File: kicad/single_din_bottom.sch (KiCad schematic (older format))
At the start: 7 parts, among them J1 Conn_01x04, J2 Conn_01x04, J3 Conn_01x04, J4 Conn_01x04, U1 R-78B3.3-2.0

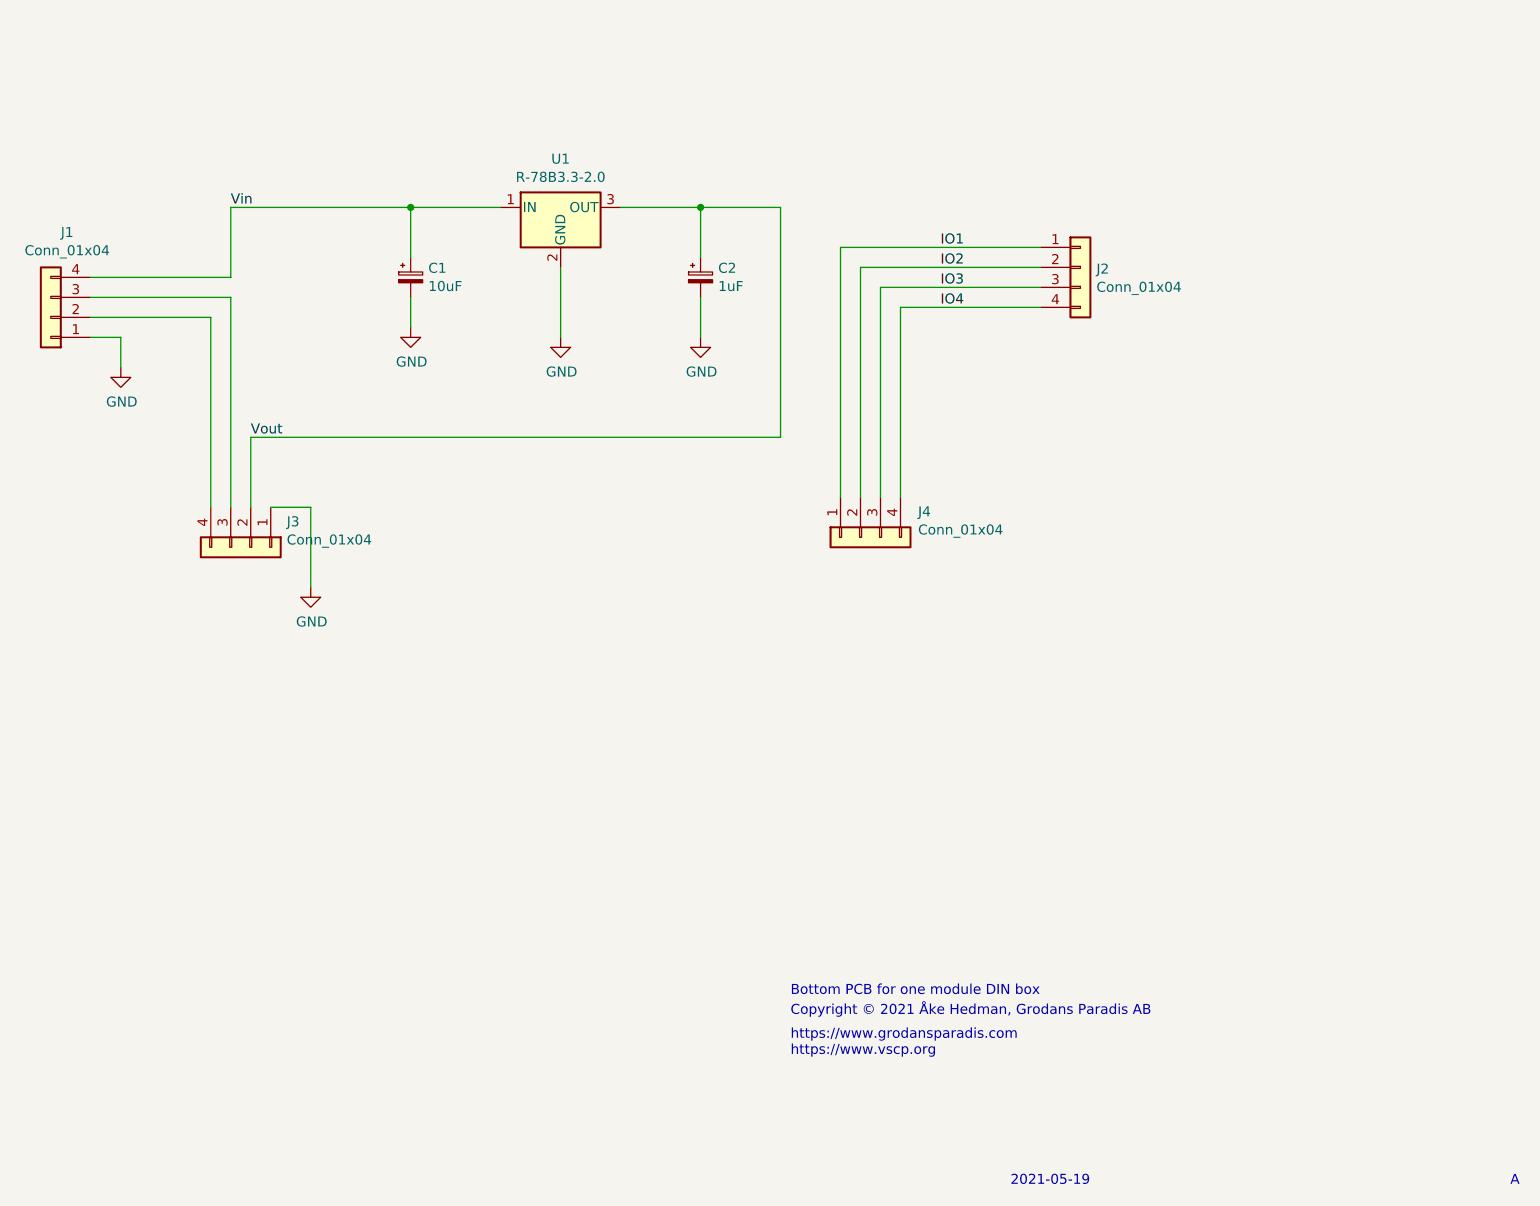
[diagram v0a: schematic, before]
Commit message: Fixed ground plane
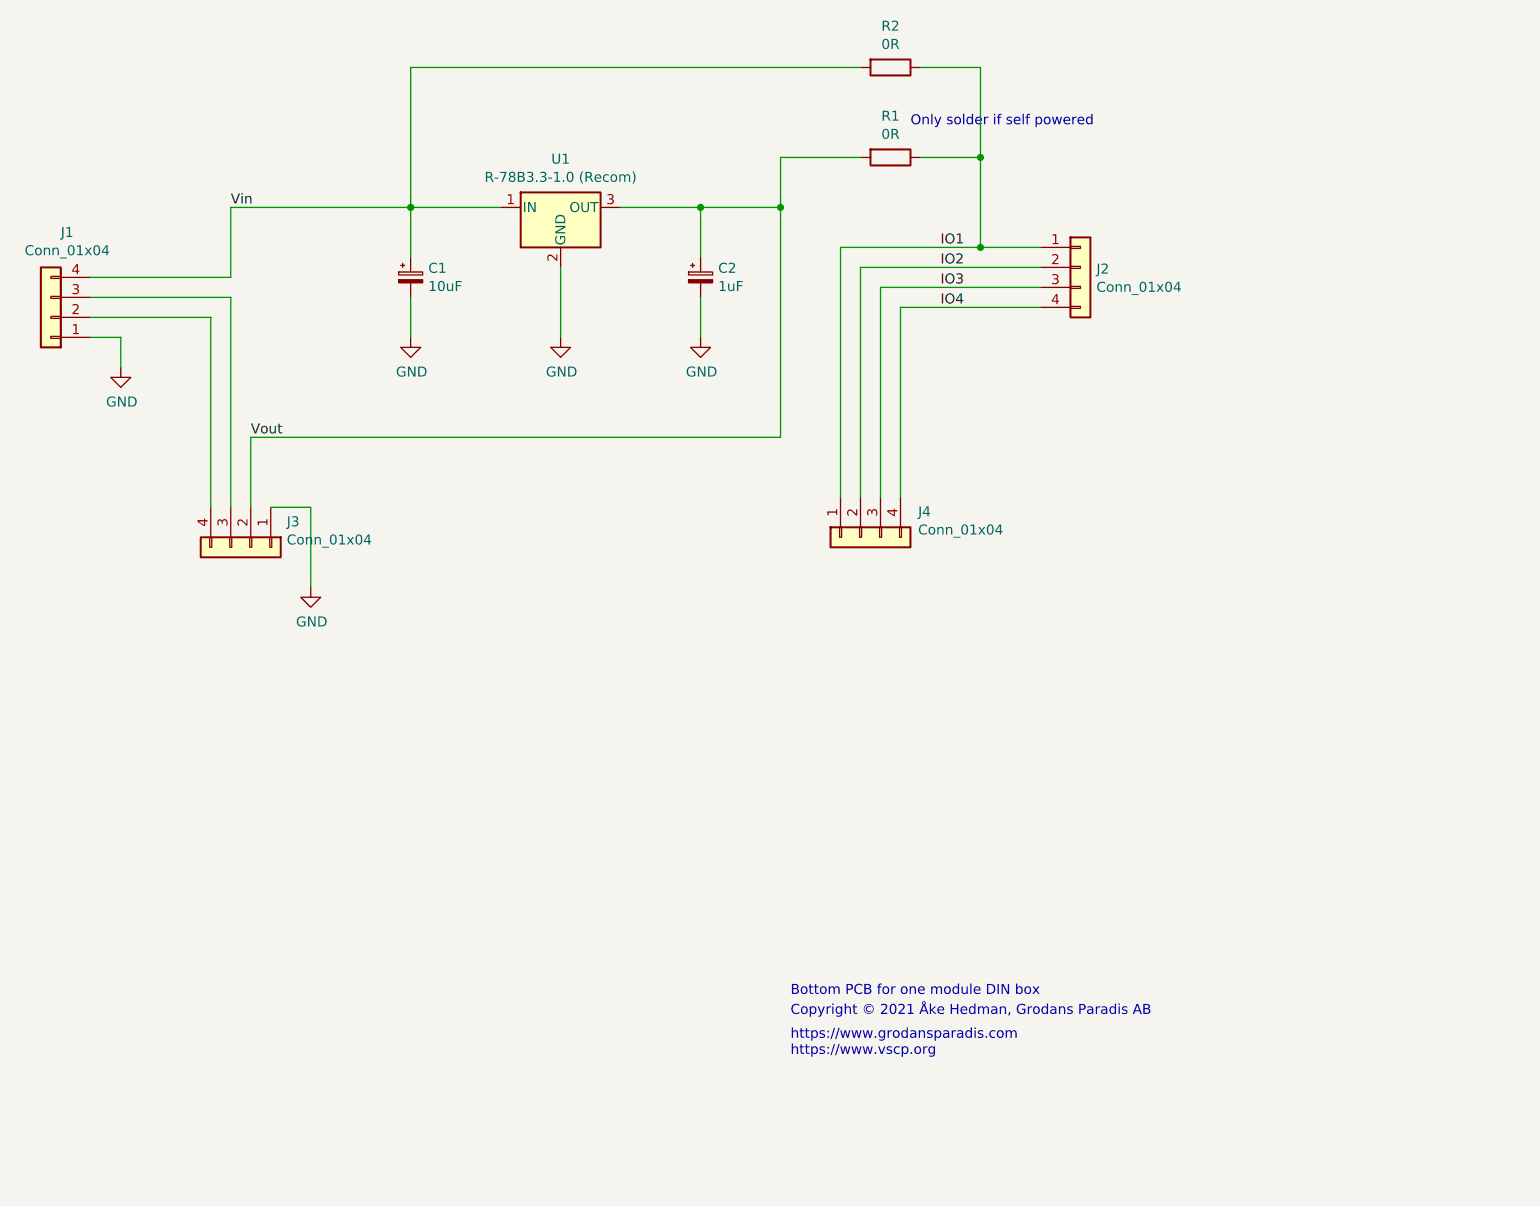
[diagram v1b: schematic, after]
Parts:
- added R1, R2: 0R, Resistor_SMD:R_0805_2012Metric, symbol Device:R
- U1: value R-78B3.3-2.0 -> R-78B3.3-1.0 (Recom)
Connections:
- net IO1: now also R1.1, R2.1
- net Vin: now also R2.2
- net Vout: now also R1.2
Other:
- note added: "Only solder if self powered"
- note removed: "2021-05-19"
- note removed: "A"
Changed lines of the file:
@@
 P 5900 2750
 F 0 "U1" H 5900 2992 50  0000 C CNN
-F 1 "R-78B3.3-2.0" H 5900 2901 50  0000 C CNN
+F 1 "R-78B3.3-1.0 (Recom)" H 5900 2901 50  0000 C CNN
 F 2 "Converter_DCDC:Converter_DCDC_RECOM_R-78B-2.0_THT" H 5950 2500 50  0001 L CIN
 F 3 "https://www.recom-power.com/pdf/Innoline/R-78Bxx-2.0.pdf" H 5900 2750 50  0001 C CNN
@@
 $EndComp
 $Comp
-L power:GND #PWR?
-U 1 1 60A5EFFA
-P 5150 3350
-F 0 "#PWR?" H 5150 3100 50  0001 C CNN
-F 1 "GND" H 5155 3177 50  0000 C CNN
-F 2 "" H 5150 3350 50  0001 C CNN
-F 3 "" H 5150 3350 50  0001 C CNN
-	1    5150 3350
-	1    0    0    -1
-$EndComp
-$Comp
-L power:GND #PWR?
+L power:GND #PWR0102
 U 1 1 60A5F63B
 P 5900 3400
-F 0 "#PWR?" H 5900 3150 50  0001 C CNN
+F 0 "#PWR0102" H 5900 3150 50  0001 C CNN
 F 1 "GND" H 5905 3227 50  0000 C CNN
 F 2 "" H 5900 3400 50  0001 C CNN
@@
 $EndComp
 $Comp
-L power:GND #PWR?
+L power:GND #PWR0103
 U 1 1 60A5FC38
 P 6600 3400
-F 0 "#PWR?" H 6600 3150 50  0001 C CNN
+F 0 "#PWR0103" H 6600 3150 50  0001 C CNN
 F 1 "GND" H 6605 3227 50  0000 C CNN
 F 2 "" H 6600 3400 50  0001 C CNN
@@
 $EndComp
 $Comp
-L power:GND #PWR?
+L power:GND #PWR0104
 U 1 1 60A67FE8
 P 3700 3550
-F 0 "#PWR?" H 3700 3300 50  0001 C CNN
+F 0 "#PWR0104" H 3700 3300 50  0001 C CNN
 F 1 "GND" H 3705 3377 50  0000 C CNN
 F 2 "" H 3700 3550 50  0001 C CNN
@@
 	3700 3400 3700 3550
 $Comp
-L power:GND #PWR?
+L power:GND #PWR0105
 U 1 1 60A69DEB
 P 4650 4650
-F 0 "#PWR?" H 4650 4400 50  0001 C CNN
+F 0 "#PWR0105" H 4650 4400 50  0001 C CNN
 F 1 "GND" H 4655 4477 50  0000 C CNN
 F 2 "" H 4650 4650 50  0001 C CNN
@@
 	7300 4200 7300 2950
 Wire Wire Line
-	7300 2950 8300 2950
+	7300 2950 8000 2950
 Wire Wire Line
 	6600 3200 6600 3400
@@
 $EndComp
 Wire Wire Line
-	5150 3200 5150 3350
+	5150 3200 5150 3400
 $Comp
 L Device:CP_Small C1
@@
 Text Label 7800 3250 0    50   ~ 0
 IO4
-Text Notes 10650 7650 0    50   ~ 0
-A
-Text Notes 8150 7650 0    50   ~ 0
-2021-05-19
+$Comp
+L Device:R R1
+U 1 1 60A6F88C
+P 7550 2500
+F 0 "R1" V 7343 2500 50  0000 C CNN
+F 1 "0R" V 7434 2500 50  0000 C CNN
+F 2 "Resistor_SMD:R_0805_2012Metric" V 7480 2500 50  0001 C CNN
+F 3 "~" H 7550 2500 50  0001 C CNN
+	1    7550 2500
+	0    1    1    0
+$EndComp
+Wire Wire Line
+	7400 2500 7000 2500
+Wire Wire Line
+	7000 2500 7000 2750
+Connection ~ 7000 2750
+Wire Wire Line
+	7700 2500 8000 2500
+Wire Wire Line
+	8000 2500 8000 2950
+Connection ~ 8000 2950
+Wire Wire Line
+	8000 2950 8300 2950
+Text Notes 7650 2350 0    50   ~ 0
+Only solder if self powered
+$Comp
+L Device:R R2
+U 1 1 60A78D1A
+P 7550 2050
+F 0 "R2" V 7343 2050 50  0000 C CNN
+F 1 "0R" V 7434 2050 50  0000 C CNN
+F 2 "Resistor_SMD:R_0805_2012Metric" V 7480 2050 50  0001 C CNN
+F 3 "~" H 7550 2050 50  0001 C CNN
+	1    7550 2050
+	0    1    1    0
+$EndComp
+Wire Wire Line
+	7700 2050 8000 2050
+Wire Wire Line
+	8000 2050 8000 2500
+Connection ~ 8000 2500
+Wire Wire Line
+	7400 2050 5150 2050
+Wire Wire Line
+	5150 2050 5150 2750
+$Comp
+L power:GND #PWR0101
+U 1 1 60A5EFFA
+P 5150 3400
+F 0 "#PWR0101" H 5150 3150 50  0001 C CNN
+F 1 "GND" H 5155 3227 50  0000 C CNN
+F 2 "" H 5150 3400 50  0001 C CNN
+F 3 "" H 5150 3400 50  0001 C CNN
+	1    5150 3400
+	1    0    0    -1
+$EndComp
 $EndSCHEMATC
